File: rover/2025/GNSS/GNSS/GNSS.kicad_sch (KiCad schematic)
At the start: 29 parts, among them J1 Eth-Horiz, J2 Eth-Horiz, J3 USB_C_USB4105-GF-A, J4 JST6_Pin, SW1 TS09-63-25-WT-160-SMT-TR, SW2 TS09-63-25-WT-160-SMT-TR, U1 SN65HVD232, U2 ESP32-S3-WROVER, U3 LD1086DT33TR, U4 LDO-LM7805MPX/NOPB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

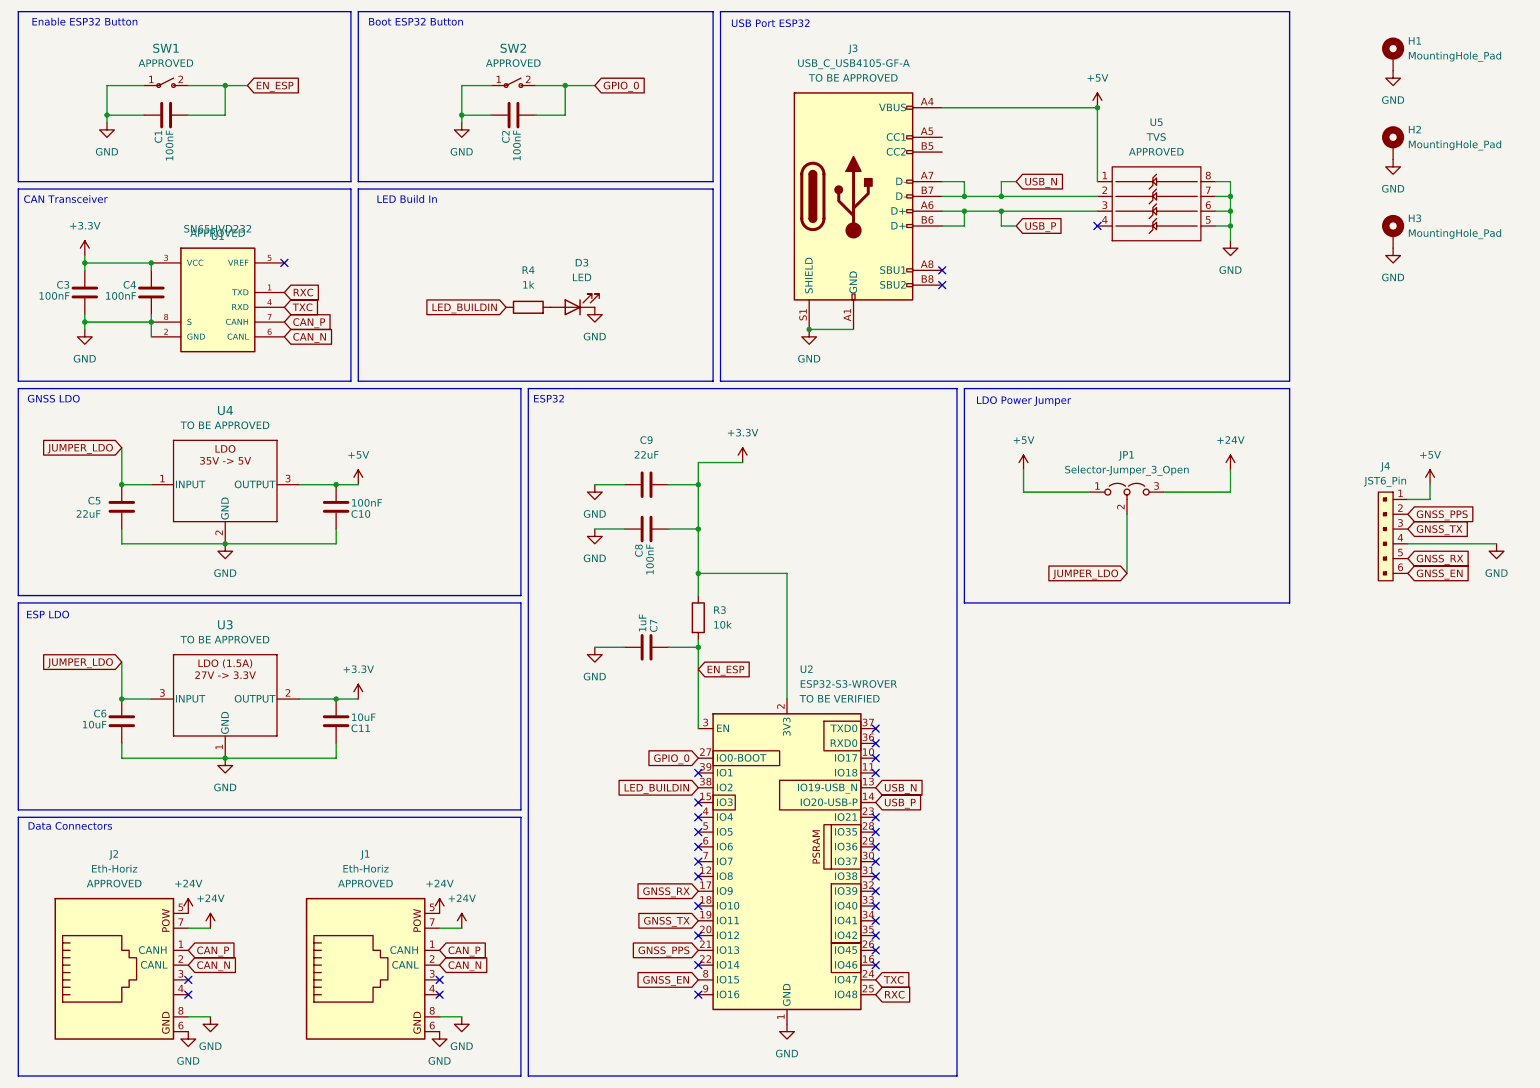
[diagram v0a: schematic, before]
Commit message: Power source jumper connections changed
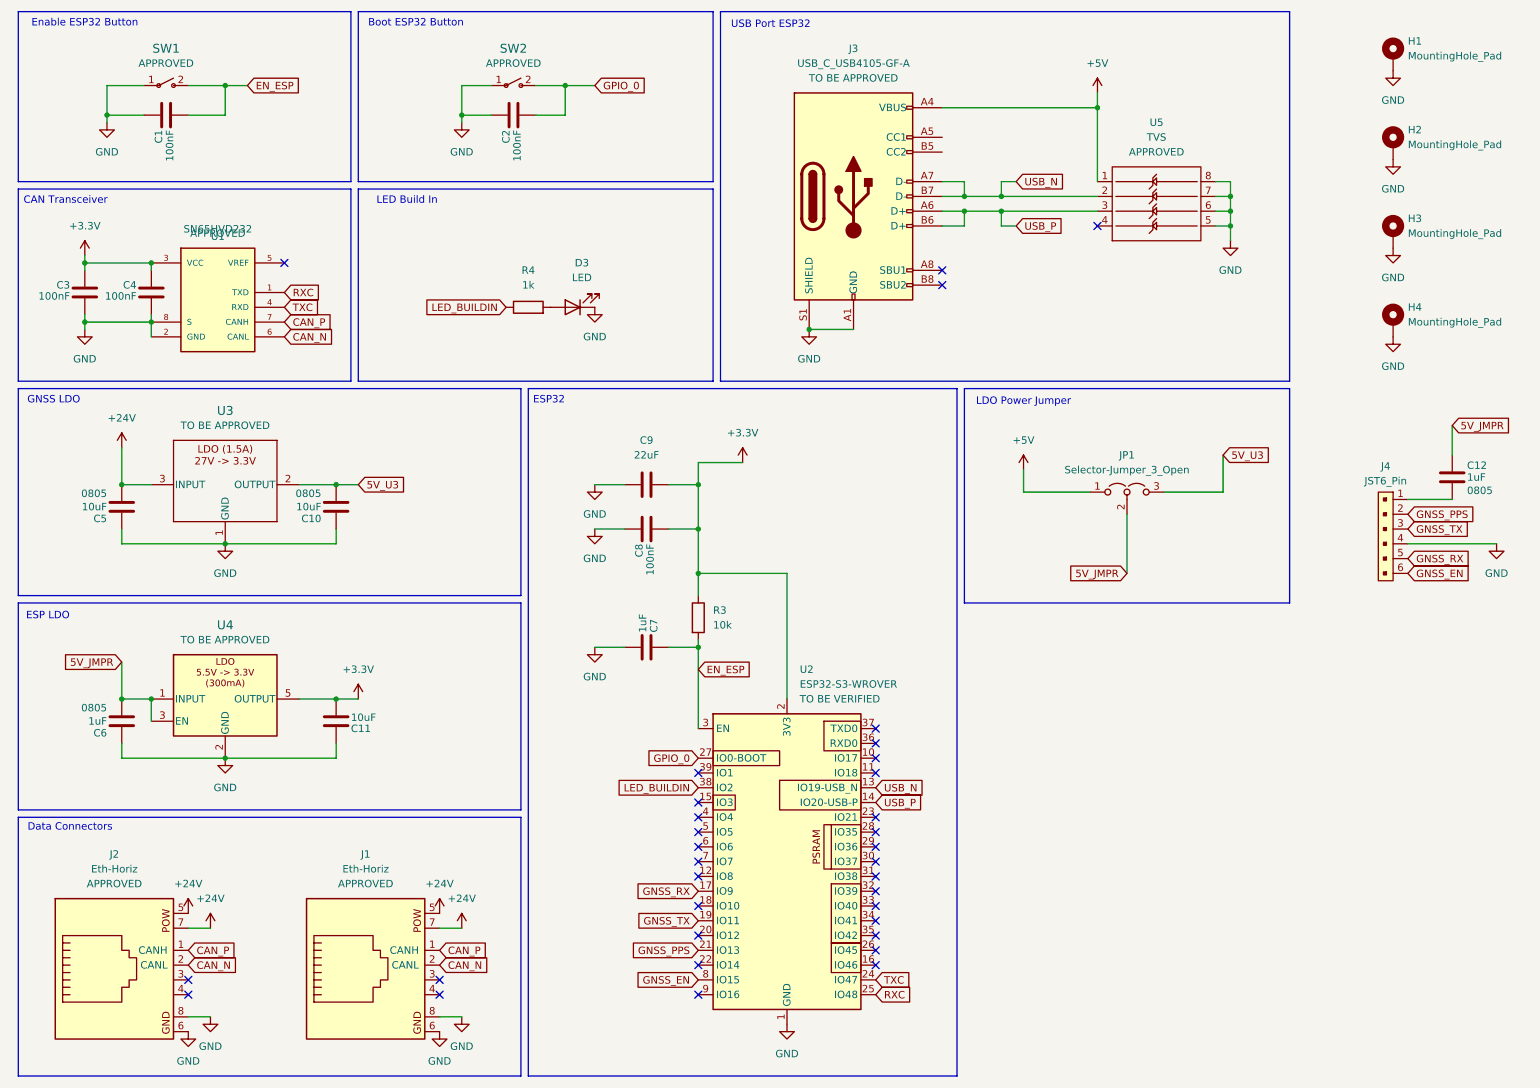
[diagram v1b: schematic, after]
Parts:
- removed C10: 100nF, Capacitor_SMD:C_0805_2012Metric_Pad1.18x1.45mm_HandSolder, symbol RoverLibrary:C-100nF
- removed C5: 22uF, Capacitor_SMD:C_0805_2012Metric_Pad1.18x1.45mm_HandSolder, symbol RoverLibrary:C-22uF
- removed C6: 10uF, Capacitor_SMD:C_0805_2012Metric_Pad1.18x1.45mm_HandSolder, symbol RoverLibrary:C-10uF
- removed U4: LDO-LM7805MPX/NOPB, Package_TO_SOT_SMD:SOT-223-3_TabPin2, symbol RoverLibrary:LDO-LM7805MPX/NOPB
- added C10, C5: 10uF, Capacitor_SMD:C_0805_2012Metric_Pad1.18x1.45mm_HandSolder, symbol RoverLibrary:C_0805
- added C12, C6: 1uF, Capacitor_SMD:C_0805_2012Metric_Pad1.18x1.45mm_HandSolder, symbol RoverLibrary:C_0805
- added H4: MountingHole_Pad, MountingHole:MountingHole_3.2mm_M3_DIN965_Pad_TopBottom, symbol RoverLibrary:MountingHole_Pad
- added U4: LDO-TLV74033PDBVR, Package_TO_SOT_SMD:SOT-23-5_HandSoldering, symbol RoverLibrary:LDO-TLV74033PDBVR
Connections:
- net +24V: now also U3.3 (INPUT), C5.2; no longer JP1.3 (B)
- net +3.3V: now also U4.5 (OUTPUT); no longer U3.2 (OUTPUT)
- net +5V: no longer J4.1
- net GND: now also C10.1, C5.1, C6.1, H4.1, U4.2 (GND)
- net JUMPER_LDO renamed 5V_JMPR
- net 5V_JMPR: now also C12.1, C6.2, U4.1 (INPUT), U4.3 (EN); no longer U3.3 (INPUT)
- new net: C12.2, J4.1
- new net 5V_U3: C10.2, JP1.3 (B), U3.2 (OUTPUT)
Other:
- moved on the sheet: U3
